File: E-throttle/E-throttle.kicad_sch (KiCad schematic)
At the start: 33 parts, among them J1 PROG, J2 JTAG, J3 Conn_01x08, M1 Stepper_Motor_bipolar, SW1 SW_Push, SW2 SW_Push, SW3 SW_Push, SW4 SW_Push, SW5 SW_Push, U1 ESP32-S3-WROOM-1-N16R8, U2 LM317_SOT-223, U3 LM317_SOT-223, U4 MCP2551-I-P, U5 MCP2515-xSO, Y1 16M

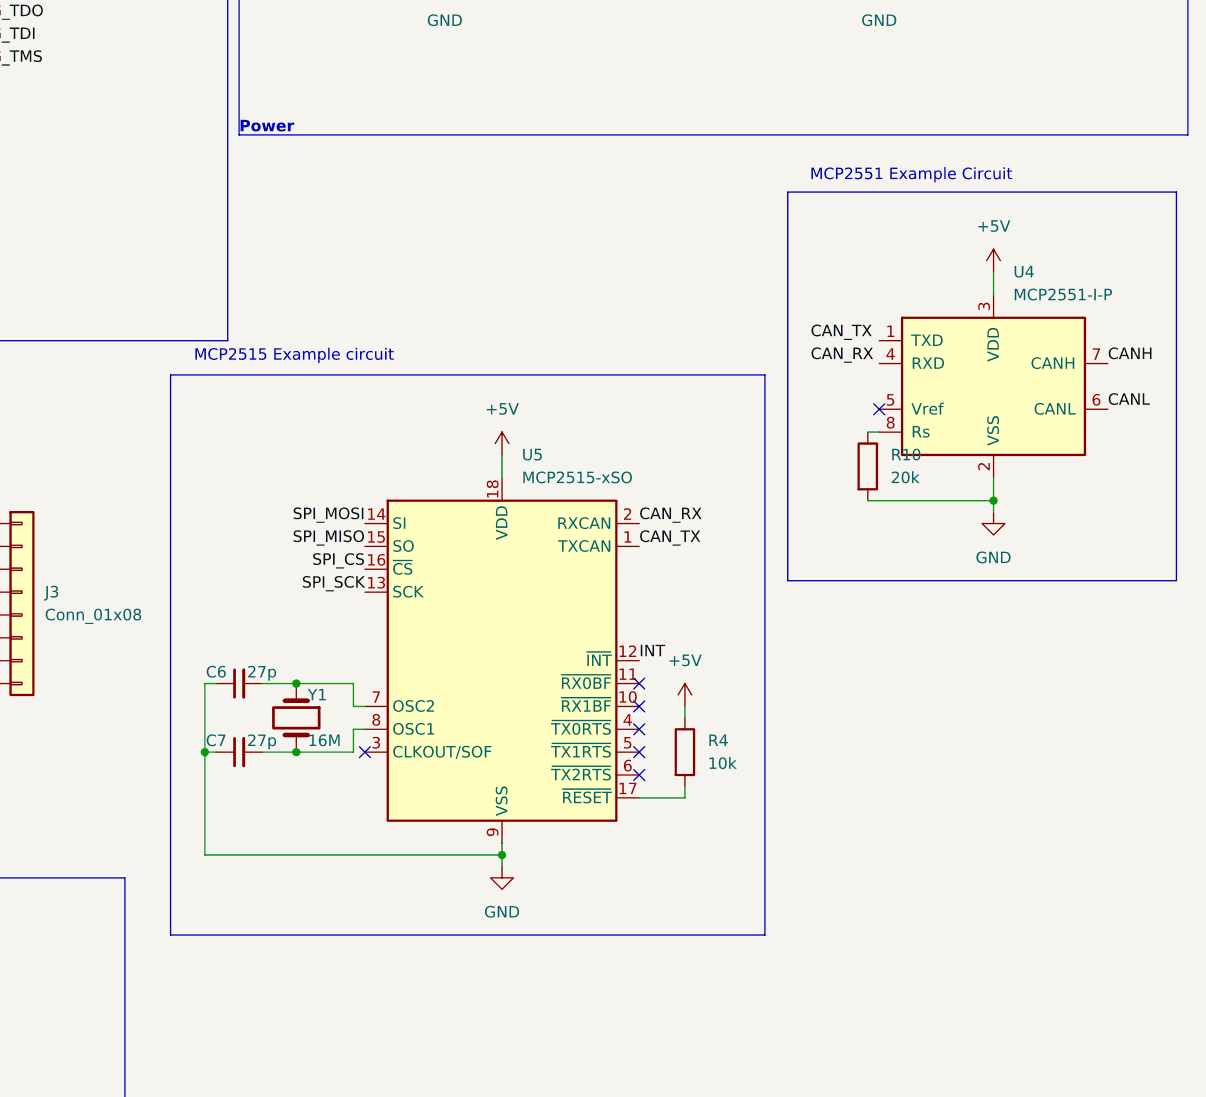
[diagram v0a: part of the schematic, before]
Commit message: Added Stepper Motor Driver (Not Integrated), Deleted CAN Bus Controller MCP2515
Added Stepper Motor Driver (Not Integrated),
Deleted CAN Bus Controller MCP2515
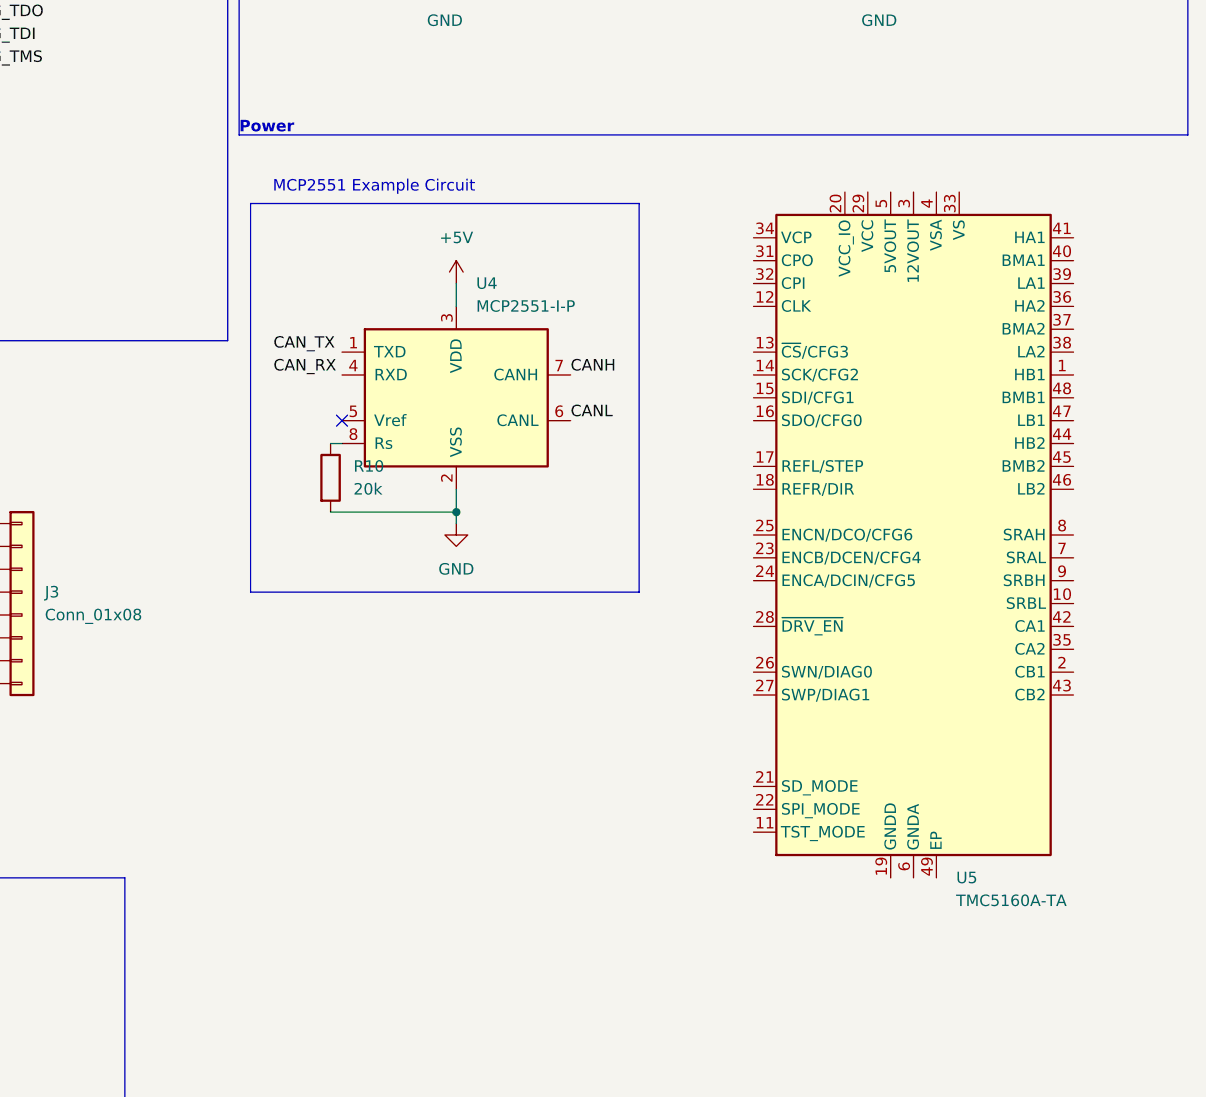
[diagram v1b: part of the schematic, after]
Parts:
- removed C6, C7: 27p, Capacitor_THT:C_Disc_D5.1mm_W3.2mm_P5.00mm, symbol Device:C_Small
- removed R4: 10k, Resistor_THT:R_Axial_DIN0207_L6.3mm_D2.5mm_P7.62mm_Horizontal, symbol Device:R
- removed U5: MCP2515-xSO, Package_DIP:DIP-18_W7.62mm, symbol Interface_CAN_LIN:MCP2515-xSO
- removed Y1: 16M, Crystal:Crystal_HC49-U_Vertical, symbol Device:Crystal
- added U5: TMC5160A-TA, Package_QFP:TQFP-48-1EP_7x7mm_P0.5mm_EP5x5mm_ThermalVias, symbol Driver_Motor:TMC5160A-TA
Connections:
- new net: U5.19 (GNDD), U5.30 (GNDD)
- no-connect marks 8 -> 2
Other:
- note removed: "MCP2515 Example circuit"
- moved on the sheet: R10, U4

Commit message: Connector Complete
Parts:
- removed J3: Conn_01x08, FBR_Footprints:TE_776280-1, symbol Connector_Generic:Conn_01x08
- removed R1, R3, R6, R7: 100k, Resistor_THT:R_Axial_DIN0207_L6.3mm_D2.5mm_P10.16mm_Horizontal, symbol Device:R_Small
- removed SW2, SW3, SW4, SW5: SW_Push, Button_Switch_THT:SW_PUSH_1P1T_6x3.5mm_H4.3_APEM_MJTP1243, symbol Switch:SW_Push
- removed U5: TMC5160A-TA, Package_QFP:TQFP-48-1EP_7x7mm_P0.5mm_EP5x5mm_ThermalVias, symbol Driver_Motor:TMC5160A-TA
- added J4: 776087-1, symbol Connector_Generic:Conn_01x23
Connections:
- net +12V: now also J4.1 (Pin_1)
- net GND: now also J4.21 (Pin_21), J4.22 (Pin_22), J4.23 (Pin_23)
- new net +12VStep: J4.2 (Pin_2)
- new net APPS-GND: J4.12 (Pin_12)
- new net APPS-PWR: J4.11 (Pin_11)
- new net APPS-SIG1: J4.13 (Pin_13)
- new net APPS-SIG2: J4.14 (Pin_14)
- new net CAN-H: J4.19 (Pin_19)
- new net CAN-L: J4.20 (Pin_20)
- new net STEP-1+: J4.15 (Pin_15)
- new net STEP-1-: J4.16 (Pin_16)
- new net STEP-2+: J4.17 (Pin_17)
- new net STEP-2-: J4.18 (Pin_18)
- new net TPS-GND1: J4.7 (Pin_7)
- new net TPS-GND2: J4.10 (Pin_10)
- new net TPS-PWR1: J4.5 (Pin_5)
- new net TPS-PWR2: J4.8 (Pin_8)
- new net TPS-SIG1: J4.6 (Pin_6)
- new net TPS-SIG2: J4.9 (Pin_9)
- new net blip: J4.4 (Pin_4)
- new net idle: J4.3 (Pin_3)

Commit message: Schematic Complete
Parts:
- removed M1: Stepper_Motor_bipolar, symbol Motor:Stepper_Motor_bipolar
- added J3, J5: Conn_01x11, symbol Connector_Generic:Conn_01x11
- added Q1: NMOS, symbol Simulation_SPICE:NMOS
- added R1: 100k, symbol Device:R_Small
- added R13, R6: 66.5k, symbol Device:R_Small
- added R3, R7: 33.2k, symbol Device:R_Small
- added R4, R5: R_Small, symbol Device:R_Small
- added RV1, RV2, RV3, RV4: 100k, symbol Device:R_Potentiometer_Small
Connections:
- net APPS-GND is gone; now on net GND: J4.12 (Pin_12)
- net APPS-PWR is gone; now on net +5V: J4.11 (Pin_11)
- net idle is gone; now on net IDLE: J4.3 (Pin_3)
- net +12V: now also R5.1
- net +12VStep: now also J5.1 (Pin_1)
- net +3V3: now also J3.1 (Pin_1), Q1.2 (G), R1.1, R4.1, RV1.1, RV2.1, RV3.1, RV4.1
- net APPS-SIG1: now also R3.1
- net APPS-SIG2: now also R7.1
- net CAN_RX: now also U4.4 (RXD)
- net CAN_TX: now also U4.1 (TXD)
- net GND: now also J3.10 (Pin_10), J3.11 (Pin_11), J3.2 (Pin_2), J3.7 (Pin_7), J3.8 (Pin_8), J3.9 (Pin_9), J5.10 (Pin_10), J5.11 (Pin_11), J5.2 (Pin_2), J5.7 (Pin_7), J5.9 (Pin_9), R13.2, R6.2, RV1.3, RV2.3, RV3.3, RV4.3
- net STEP-1+: now also J5.6 (Pin_6)
- net STEP-1-: now also J5.5 (Pin_5)
- net STEP-2+: now also J5.4 (Pin_4)
- net STEP-2-: now also J5.3 (Pin_3)
- net TPS-GND1: now also RV2.2
- net TPS-GND2: now also RV4.2
- net TPS-PWR1: now also RV1.2
- net TPS-PWR2: now also RV3.2
- net TPS-SIG1: now also U1.5 (IO5)
- net TPS-SIG2: now also U1.6 (IO6)
- net BLIP-OUT: now reaches U1.10 (IO17)
- net BLIP-OUT: now also Q1.3 (S), R4.2
- net IDLE: now reaches U1.11 (IO18)
- net IDLE: now also R1.2
- net APPS-SIG1-OUT: now reaches U1.15 (IO3)
- net APPS-SIG1-OUT: now also R3.2, R6.1
- net SPI-CS: now reaches U1.17 (IO9)
- net SPI-CS: now also J3.3 (Pin_3)
- net SPI-SCK: now reaches U1.18 (IO10)
- net SPI-SCK: now also J3.4 (Pin_4)
- net APPS-SIG2-OUT: now reaches U1.4 (IO4)
- net APPS-SIG2-OUT: now also R13.1, R7.2
- net SW2 renamed SPI-MOSI
- net SPI-MOSI: now also J3.5 (Pin_5)
- net SW3 renamed SPI-MISO
- net SPI-MISO: now also J3.6 (Pin_6)
- net SW4 renamed DIAG0
- net DIAG0: now also J5.8 (Pin_8)
- net SW5: no longer names the net of U1.22 (IO14)
- net blip renamed BLIP-IN
- net BLIP-IN: now also Q1.1 (D), R5.2
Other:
- note added: "APPS"
- note added: "BLIP"
- note added: "IDLE"
- note added: "Main Connector"
- note added: "TPS"
- note added: "VCC_IO GND CS SCK MOSI MISO GND CLK16 EN REFL REFR"
- note added: "VStep GND B2 B1 A2 A1 GND DIAG0 ENCA ENCB ENCN"
- moved on the sheet: J4, R10, U4

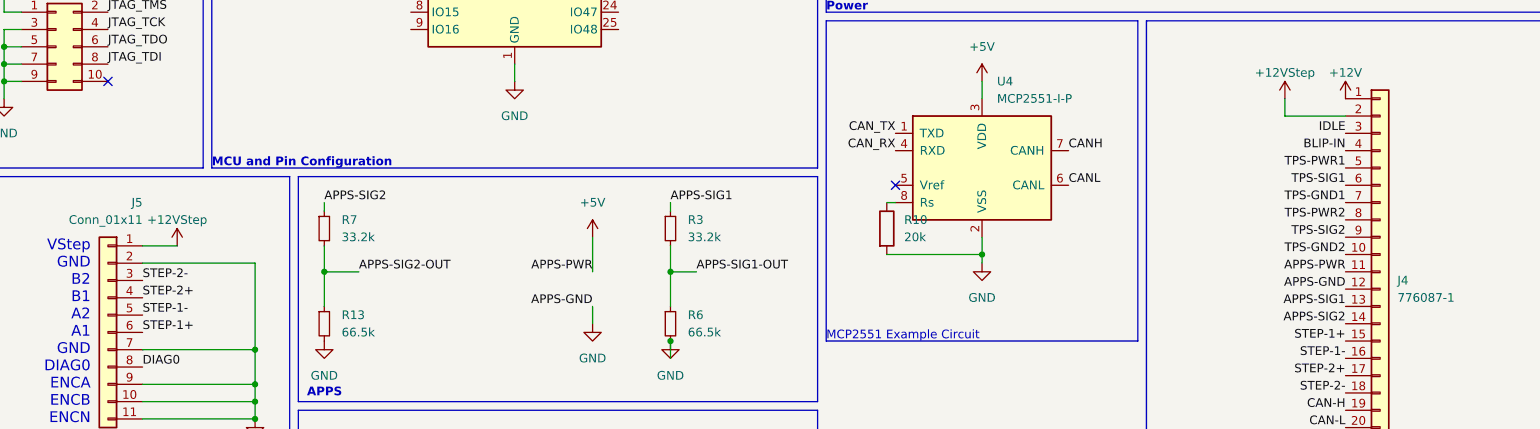
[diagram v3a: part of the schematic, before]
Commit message: Footprint Complete
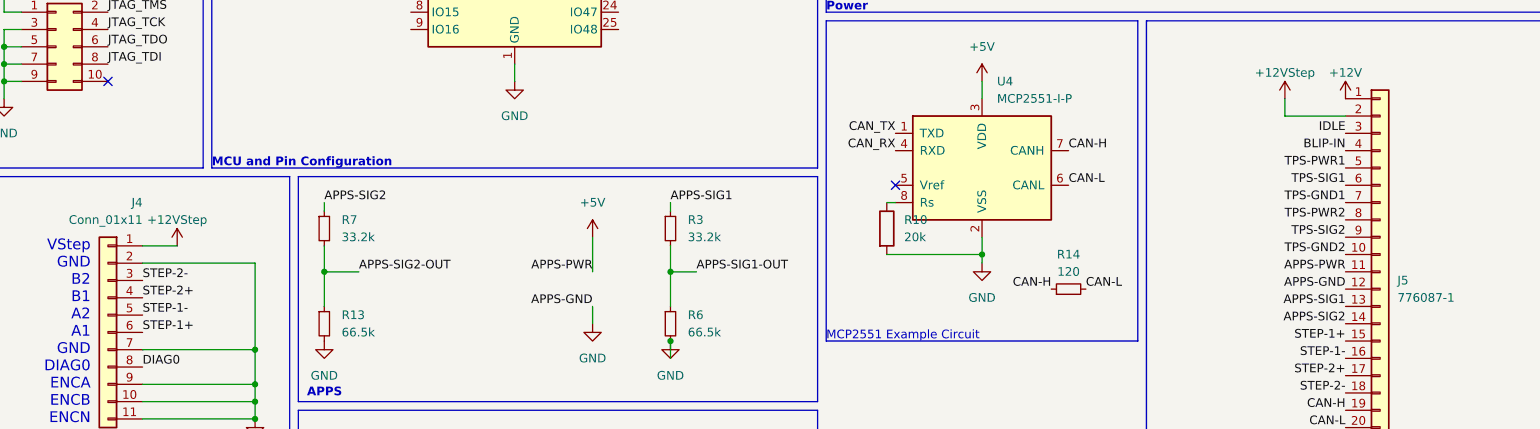
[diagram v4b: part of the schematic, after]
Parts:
- added R14: 120, Resistor_THT:R_Axial_DIN0207_L6.3mm_D2.5mm_P10.16mm_Horizontal, symbol Device:R_Small
- J3: footprint (none) -> Connector_PinHeader_2.54mm:PinHeader_1x11_P2.54mm_Vertical
- J4: renamed from J5; footprint (none) -> Connector_PinHeader_2.54mm:PinHeader_1x11_P2.54mm_Vertical
- J5: renamed from J4; footprint (none) -> FBR_Footprints:TE_776087-1
- Q1: footprint (none) -> Package_TO_SOT_SMD:TO-263-3_TabPin2
- R1, R13, R3, R4, R5, R6, R7: footprint (none) -> Resistor_THT:R_Axial_DIN0207_L6.3mm_D2.5mm_P10.16mm_Horizontal
- R10: footprint Resistor_THT:R_Axial_DIN0207_L6.3mm_D2.5mm_P7.62mm_Horizontal -> Resistor_THT:R_Axial_DIN0207_L6.3mm_D2.5mm_P10.16mm_Horizontal
- RV1, RV2, RV3, RV4: footprint (none) -> Potentiometer_THT:Potentiometer_Bourns_3296Y_Vertical
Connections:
- net CANH is gone; now on net CAN-H: U4.7 (CANH)
- net CANL is gone; now on net CAN-L: U4.6 (CANL)
- net CAN-H: now also R14.1
- net CAN-L: now also R14.2
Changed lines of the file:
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@@
 		)
 	)
+	(label "CAN-L"
+		(at 217.17 115.57 0)
+		(fields_autoplaced yes)
+		(effects
+			(font
+				(size 1.27 1.27)
+			)
+			(justify left bottom)
+		)
+	)
 	(label "UART_RX"
 		(at 24.13 80.01 180)
@@
 		)
 	)
-	(label "CANH"
+	(label "CAN-H"
 		(at 214.63 95.25 0)
 		(fields_autoplaced yes)
@@
 		)
 	)
-	(label "CANL"
+	(label "CAN-L"
 		(at 214.63 100.33 0)
 		(fields_autoplaced yes)
@@
 		)
 	)
+	(label "CAN-H"
+		(at 212.09 115.57 180)
+		(fields_autoplaced yes)
+		(effects
+			(font
+				(size 1.27 1.27)
+			)
+			(justify right bottom)
+		)
+	)
 	(symbol
 		(lib_id "Device:R")
@@
 			)
 		)
-		(property "Footprint" "Resistor_THT:R_Axial_DIN0207_L6.3mm_D2.5mm_P7.62mm_Horizontal"
+		(property "Footprint" "Resistor_THT:R_Axial_DIN0207_L6.3mm_D2.5mm_P10.16mm_Horizontal"
 			(at 186.182 106.68 90)
 			(effects
@@
 			)
 		)
-		(property "Footprint" ""
+		(property "Footprint" "Package_TO_SOT_SMD:TO-263-3_TabPin2"
 			(at 38.1 176.53 0)
 			(effects
@@
 		(on_board yes)
 		(dnp no)
-		(property "Reference" "J5"
+		(property "Reference" "J4"
 			(at 78.74 102.87 0)
 			(effects
@@
 			)
 		)
-		(property "Footprint" ""
+		(property "Footprint" "Connector_PinHeader_2.54mm:PinHeader_1x11_P2.54mm_Vertical"
 			(at 73.66 121.92 0)
 			(effects
@@
 			(project "E-throttle"
 				(path "/6e34869e-da06-4d64-b4b2-885b48fe3f81"
-					(reference "J5")
+					(reference "J4")
 					(unit 1)
 				)
@@
 			)
 		)
-		(property "Footprint" ""
+		(property "Footprint" "Resistor_THT:R_Axial_DIN0207_L6.3mm_D2.5mm_P10.16mm_Horizontal"
 			(at 156.21 120.65 0)
 			(effects
@@
 			)
 		)
-		(property "Footprint" ""
+		(property "Footprint" "Resistor_THT:R_Axial_DIN0207_L6.3mm_D2.5mm_P10.16mm_Horizontal"
 			(at 105.41 106.68 0)
 			(effects
@@
 			)
 		)
-		(property "Footprint" ""
+		(property "Footprint" "Resistor_THT:R_Axial_DIN0207_L6.3mm_D2.5mm_P10.16mm_Horizontal"
 			(at 71.12 166.37 0)
 			(effects
@@
 			)
 		)
-		(property "Footprint" ""
+		(property "Footprint" "Resistor_THT:R_Axial_DIN0207_L6.3mm_D2.5mm_P10.16mm_Horizontal"
 			(at 156.21 106.68 0)
 			(effects
@@
 			)
 		)
-		(property "Footprint" ""
+		(property "Footprint" "Connector_PinHeader_2.54mm:PinHeader_1x11_P2.54mm_Vertical"
 			(at 41.91 121.92 0)
 			(effects
@@
 			)
 		)
-		(property "Footprint" ""
+		(property "Footprint" "Potentiometer_THT:Potentiometer_Bourns_3296Y_Vertical"
 			(at 146.05 148.59 0)
 			(effects
@@
 		(dnp no)
 		(fields_autoplaced yes)
-		(property "Reference" "J4"
+		(property "Reference" "J5"
 			(at 262.89 114.2999 0)
 			(effects
@@
 			)
 		)
-		(property "Footprint" ""
+		(property "Footprint" "FBR_Footprints:TE_776087-1"
 			(at 260.35 115.57 0)
 			(effects
@@
 			(project ""
 				(path "/6e34869e-da06-4d64-b4b2-885b48fe3f81"
-					(reference "J4")
+					(reference "J5")
 					(unit 1)
 				)
@@
 			)
 		)
-		(property "Footprint" ""
+		(property "Footprint" "Resistor_THT:R_Axial_DIN0207_L6.3mm_D2.5mm_P10.16mm_Horizontal"
 			(at 105.41 120.65 0)
 			(effects
@@
 			)
 		)
-		(property "Footprint" ""
+		(property "Footprint" "Resistor_THT:R_Axial_DIN0207_L6.3mm_D2.5mm_P10.16mm_Horizontal"
 			(at 25.4 167.64 0)
 			(effects
@@
 	(symbol
 		(lib_id "Device:R_Small")
+		(at 214.63 115.57 90)
+		(unit 1)
+		(exclude_from_sim no)
+		(in_bom yes)
+		(on_board yes)
+		(dnp no)
+		(fields_autoplaced yes)
+		(property "Reference" "R14"
+			(at 214.63 110.49 90)
+			(effects
+				(font
+					(size 1.27 1.27)
+				)
+			)
+		)
+		(property "Value" "120"
+			(at 214.63 113.03 90)
+			(effects
+				(font
+					(size 1.27 1.27)
+				)
+			)
+		)
+		(property "Footprint" "Resistor_THT:R_Axial_DIN0207_L6.3mm_D2.5mm_P10.16mm_Horizontal"
+			(at 214.63 115.57 0)
+			(effects
+				(font
+					(size 1.27 1.27)
+				)
+				(hide yes)
+			)
+		)
+		(property "Datasheet" "~"
+			(at 214.63 115.57 0)
+			(effects
+				(font
+					(size 1.27 1.27)
+				)
+				(hide yes)
+			)
+		)
+		(property "Description" "Resistor, small symbol"
+			(at 214.63 115.57 0)
+			(effects
+				(font
+					(size 1.27 1.27)
+				)
+				(hide yes)
+			)
+		)
+		(pin "2"
+		)
+		(pin "1"
+		)
+		(instances
+			(project ""
+				(path "/6e34869e-da06-4d64-b4b2-885b48fe3f81"
+					(reference "R14")
+					(unit 1)
+				)
+			)
+		)
+	)
+	(symbol
+		(lib_id "Device:R_Small")
 		(at 250.19 52.07 0)
 		(unit 1)
@@
 			)
 		)
-		(property "Footprint" ""
+		(property "Footprint" "Potentiometer_THT:Potentiometer_Bourns_3296Y_Vertical"
 			(at 113.03 148.59 0)
 			(effects
@@
 			)
 		)
-		(property "Footprint" ""
+		(property "Footprint" "Potentiometer_THT:Potentiometer_Bourns_3296Y_Vertical"
 			(at 129.54 148.59 0)
 			(effects
@@
 			)
 		)
-		(property "Footprint" ""
+		(property "Footprint" "Potentiometer_THT:Potentiometer_Bourns_3296Y_Vertical"
 			(at 161.29 148.59 0)
 			(effects
@@
 			)
 		)
-		(property "Footprint" ""
+		(property "Footprint" "Resistor_THT:R_Axial_DIN0207_L6.3mm_D2.5mm_P10.16mm_Horizontal"
 			(at 46.99 167.64 0)
 			(effects
